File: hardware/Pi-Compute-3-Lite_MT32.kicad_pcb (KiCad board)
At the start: 2 copper layers, 76.2 x 104.1 mm, 70 parts, among them J1 USB_B_Micro, J2 Conn_Coaxial_x2, J3 MIDI-IN, J4 MIDI-IN, J5 HD44780, J6 OLED, J7 Barrel_Jack, J8 Buttons, U1 DDR2_SODIMM_CM_3_Lite, U2 PAM2306AYPKE, U3 AP7115-25SEG, U4 PCM5102, U6 H11L1, U7 H11L1

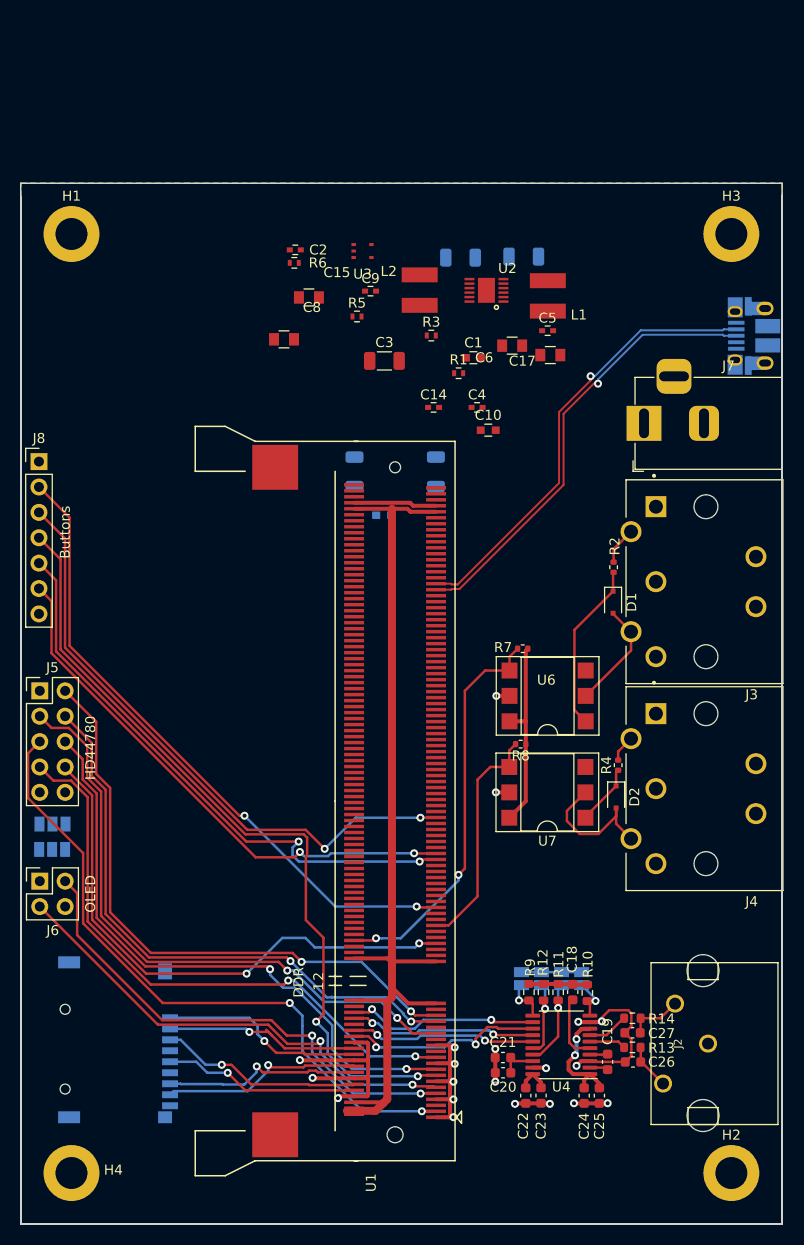
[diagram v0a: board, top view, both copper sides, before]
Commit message: Cleaning up the power section
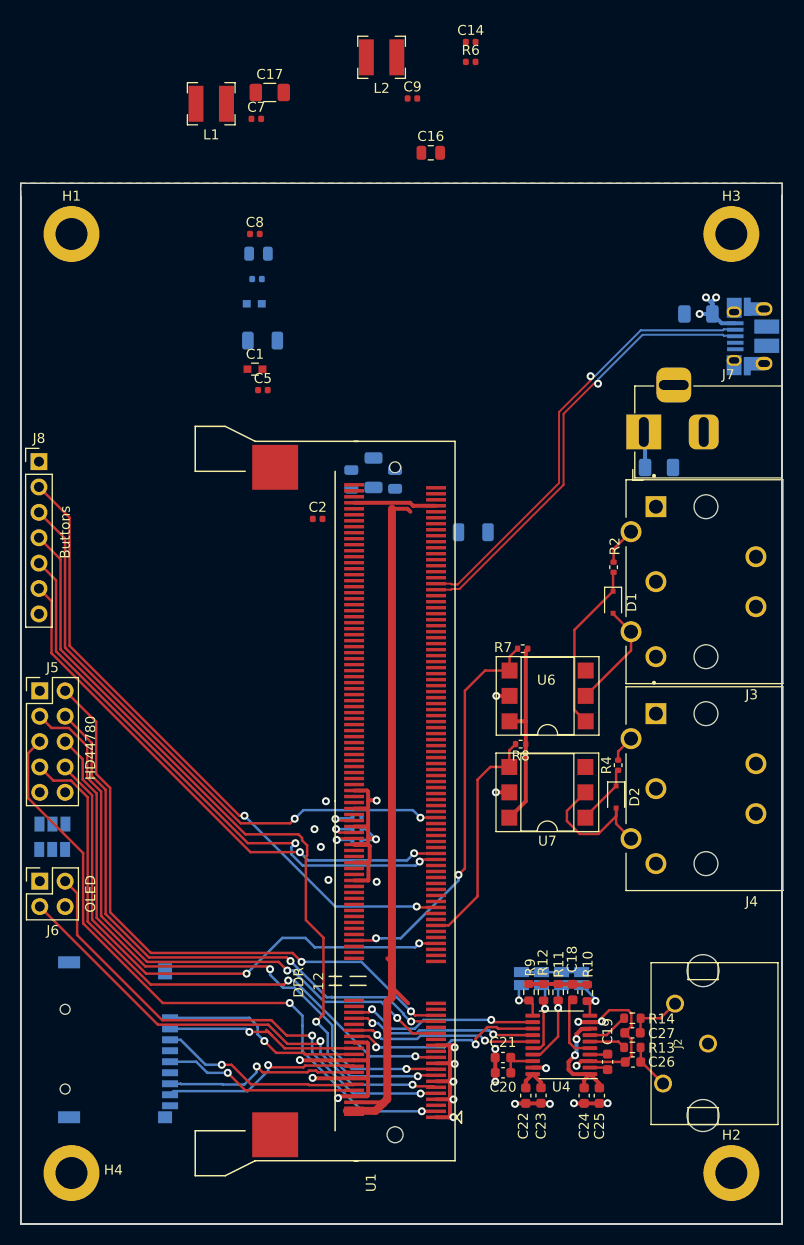
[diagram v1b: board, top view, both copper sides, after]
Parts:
- removed U2: PAM2306AYPKE, Pi-Library:PAM2306AYPKE
- removed U3: AP7115-25SEG, Pi-Library:AP7115-25SEG-7
- added C30: 47uF, Capacitor_SMD:C_1206_3216Metric, B.Cu at (122.3, 53.8)
- added C31: 47uF, Capacitor_SMD:C_1206_3216Metric, B.Cu at (126.2, 38.5)
- C10, R1, R3, R5: moved to B.Cu
- C14: value 100nF -> 4.7uF; footprint Capacitors_SMD:C_0402 -> Capacitor_SMD:C_0402_1005Metric
- C15, C6: footprint Capacitors_SMD:C_0805 -> Capacitor_SMD:C_0805_2012Metric; moved to B.Cu
- C16: value 4.7uF -> 10uF; footprint Capacitors_SMD:C_0603 -> Capacitor_SMD:C_0805_2012Metric; moved to F.Cu
- C17: value 10uF -> 47uF; footprint Capacitors_SMD:C_0805 -> Capacitor_SMD:C_1206_3216Metric
- C2, C5: footprint Capacitors_SMD:C_0402 -> Capacitor_SMD:C_0402_1005Metric
- C3: value 47uF -> 10uF; footprint Capacitor_SMD:C_1206_3216Metric -> Capacitor_SMD:C_0805_2012Metric; moved to B.Cu
- C4: footprint Capacitors_SMD:C_0402 -> Capacitor_SMD:C_0402_1005Metric; moved to B.Cu
- C7: value 47uF -> 100nF; footprint Capacitor_SMD:C_1206_3216Metric -> Capacitor_SMD:C_0402_1005Metric; moved to F.Cu
- C8: value 10uF -> 1uF; footprint Capacitors_SMD:C_0805 -> Capacitor_SMD:C_0402_1005Metric
- C9: value 1uF -> 100nF; footprint Capacitors_SMD:C_0402 -> Capacitor_SMD:C_0402_1005Metric
- L1, L2: footprint Pi-Library:SRN4018-4R7M -> Inductor_SMD:L_Bourns-SRN4018
- R6: footprint Resistors_SMD:R_0402 -> Resistor_SMD:R_0402_1005Metric
- moved R5 52.4 mm to (92.1, 91.1)
- moved R3 50.0 mm to (92.1, 90.0)
- moved R1 45.7 mm to (92.1, 89.0)
- moved C7 39.6 mm to (82.0, 19.0), turned to 0 degrees
- moved L1 38.8 mm to (77.5, 17.4), turned to 0 degrees
- moved C17 38.5 mm to (83.3, 16.3), turned to 0 degrees
- moved C14 36.8 mm to (103.5, 11.3)
- moved C16 36.6 mm to (99.5, 22.4)
- moved C5 29.1 mm to (82.7, 46.1)
- moved C13 28.0 mm to (103.7, 60.3)
- moved C2 27.0 mm to (88.1, 59.0)
- moved R6 26.8 mm to (103.5, 13.3), turned to 0 degrees
- moved C10 26.6 mm to (81.8, 37.5)
- moved C4 25.5 mm to (82.1, 35.0), turned to 180 degrees
- moved L2 23.6 mm to (94.5, 12.8), turned to 0 degrees
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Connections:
- C11 pad 1: 5V -> CM_VBAT
- C12 pad 1: 3V3 -> CM_3V3
- C13 pad 1: 1V8 -> CM_1V8
- C14 pad 1: Net-(C14-Pad1) -> (no net)
- C15 pad 1: 1V8 -> CM_3V3
- C16 pad 1: CM_VDAC -> CM_1V8
- C17 pad 1: 3V3 -> (no net)
- C2 pad 1: Net-(C2-Pad1) -> CM_VDAC
- C3 pad 1: 5V -> CM_VBAT
- C4 pad 1: 3V3 -> CM_3V3
- C5 pad 1: 3V3 -> CM_3V3
- C6 pad 1: 5V -> CM_VBAT
- C7 pad 1: 5V -> Net-(C7-Pad1)
- C8 pad 1: 5V -> 3V3
- C9 pad 1: 3V3 -> (no net)
- J1 pad 1: 5V -> CM_VBAT
- J7 pad 1: 5V -> CM_VBAT
- J8 pad 1: +3V3 -> CM_3V3
- JP5 pad 1: +3V3 -> CM_3V3
- JP5 pad 3: 5V -> +5V
- JP6 pad 1: +3V3 -> CM_3V3
- JP6 pad 3: 5V -> +5V
- L1 pad 1: Net-(L1-Pad1) -> (no net)
- L1 pad 2: 3V3 -> CM_3V3
- L2 pad 1: Net-(L2-Pad1) -> (no net)
- L2 pad 2: 1V8 -> CM_1V8
- R1 pad 2: 1V8 -> (no net)
- R6 pad 1: 5V -> CM_VBAT
- R6 pad 2: Net-(C2-Pad1) -> Net-(C7-Pad1)
- R7 pad 1: +3V3 -> CM_3V3
- R8 pad 1: +3V3 -> CM_3V3
- U1 pad 183: 1V8 -> CM_1V8
- U1 pad 184: 1V8 -> CM_1V8
- U1 pad 185: 1V8 -> CM_1V8
- U1 pad 186: 1V8 -> CM_1V8
- U1 pad 191: 3V3 -> CM_3V3
- U1 pad 192: 3V3 -> CM_3V3
- U1 pad 193: 3V3 -> CM_3V3
- U1 pad 194: 3V3 -> CM_3V3
- U1 pad 197: 5V -> CM_VBAT
- U1 pad 198: 5V -> CM_VBAT
- U1 pad 199: 5V -> CM_VBAT
- U1 pad 200: 5V -> CM_VBAT
- U1 pad 39: 3V3 -> CM_3V3
- U1 pad 40: 3V3 -> CM_3V3
- U1 pad 41: 3V3 -> CM_3V3
- U1 pad 42: 3V3 -> CM_3V3
- U6 pad 6: +3V3 -> CM_3V3
- U7 pad 6: +3V3 -> CM_3V3
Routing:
- net 3V3: track 100.8 -> 72.3 mm
- net CM_3V3: track 0.00 -> 27.6 mm
- net GND: track 76.9 -> 100.8 mm, vias 20 -> 27
- net +3V3: track 19.3 -> 0.00 mm
- net CM_VBAT: track 0.00 -> 11.3 mm, vias 0 -> 3
- net Net-(R1-Pad1): track 0.00 -> 3.67 mm, vias 0 -> 1
- net Net-(R3-Pad1): track 0.00 -> 3.60 mm, vias 0 -> 1
- net Net-(R5-Pad1): track 0.00 -> 3.38 mm, vias 0 -> 1
- net /Raspberry  PI CM3+/UX_B2: track 61.4 -> 60.0 mm
